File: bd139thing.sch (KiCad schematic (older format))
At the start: 24 parts, among them J1 Audio-Jack-3, J2 Jack-DC, Q1 PN2222, Q2 BD13916, Q3 BD13916, Q4 PN2222, Q5 BD13916, Q6 BD13916

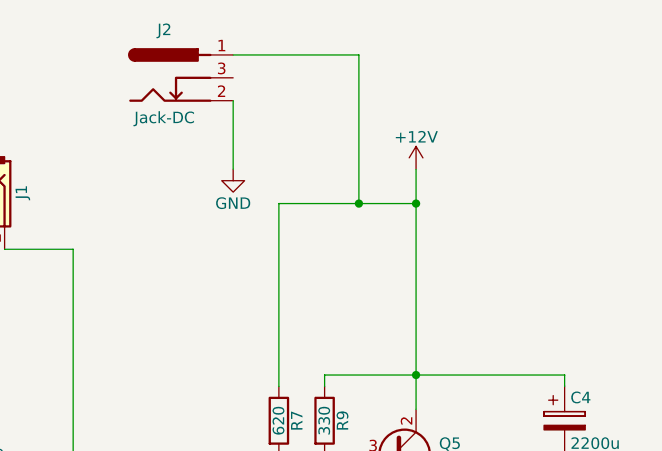
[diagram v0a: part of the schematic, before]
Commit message: r5p0 ok, improved placement on 75x75mm
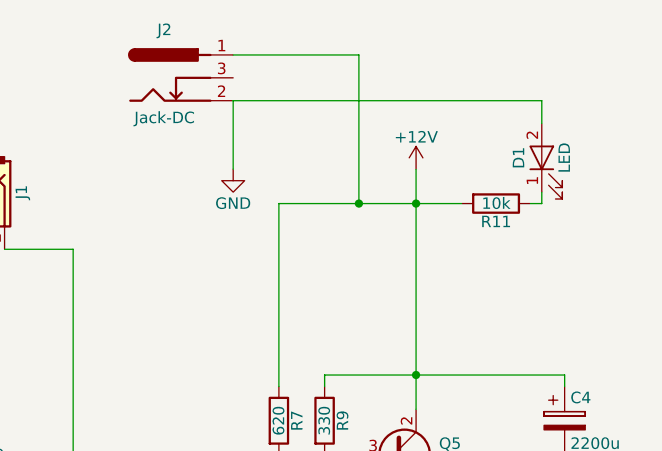
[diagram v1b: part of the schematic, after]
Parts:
- added D1: LED, LEDs:LED_D5.0mm, symbol LED
- added R11: 10k, Resistors_Universal:Resistor_SMD+THTuniversal_0805to1206_RM10_HandSoldering, symbol R
- R1, R2, R3, R4, R6, R7, R8, R9: footprint Resistors_Universal:Resistor_SMD+THTuniversal_0805to2512_RM10_HandSoldering -> Resistors_Universal:Resistor_SMD+THTuniversal_0805to1206_RM10_HandSoldering
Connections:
- net +12V: now also R11.2
- net GND: now also D1.2 (A)
- new net: D1.1 (K), R11.1
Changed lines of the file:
@@
 LIBS:contrib
 LIBS:valves
+LIBS:bd139thing-cache
 EELAYER 25 0
 EELAYER END
@@
 F 0 "R4" V 3080 3350 50  0000 C CNN
 F 1 "330" V 3000 3350 50  0000 C CNN
-F 2 "Resistors_Universal:Resistor_SMD+THTuniversal_0805to2512_RM10_HandSoldering" V 2930 3350 50  0001 C CNN
+F 2 "Resistors_Universal:Resistor_SMD+THTuniversal_0805to1206_RM10_HandSoldering" V 2930 3350 50  0001 C CNN
 F 3 "" H 3000 3350 50  0001 C CNN
 	1    3000 3350
@@
 F 0 "R2" V 2880 3350 50  0000 C CNN
 F 1 "620" V 2800 3350 50  0000 C CNN
-F 2 "Resistors_Universal:Resistor_SMD+THTuniversal_0805to2512_RM10_HandSoldering" V 2730 3350 50  0001 C CNN
+F 2 "Resistors_Universal:Resistor_SMD+THTuniversal_0805to1206_RM10_HandSoldering" V 2730 3350 50  0001 C CNN
 F 3 "" H 2800 3350 50  0001 C CNN
 	1    2800 3350
@@
 F 0 "R3" V 2880 4350 50  0000 C CNN
 F 1 "2.2k" V 2800 4350 50  0000 C CNN
-F 2 "Resistors_Universal:Resistor_SMD+THTuniversal_0805to2512_RM10_HandSoldering" V 2730 4350 50  0001 C CNN
+F 2 "Resistors_Universal:Resistor_SMD+THTuniversal_0805to1206_RM10_HandSoldering" V 2730 4350 50  0001 C CNN
 F 3 "" H 2800 4350 50  0001 C CNN
 	1    2800 4350
@@
 F 0 "R1" V 2580 3750 50  0000 C CNN
 F 1 "11" V 2500 3750 50  0000 C CNN
-F 2 "Resistors_Universal:Resistor_SMD+THTuniversal_0805to2512_RM10_HandSoldering" V 2430 3750 50  0001 C CNN
+F 2 "Resistors_Universal:Resistor_SMD+THTuniversal_0805to1206_RM10_HandSoldering" V 2430 3750 50  0001 C CNN
 F 3 "" H 2500 3750 50  0001 C CNN
 	1    2500 3750
@@
 F 0 "R9" V 5730 3300 50  0000 C CNN
 F 1 "330" V 5650 3300 50  0000 C CNN
-F 2 "Resistors_Universal:Resistor_SMD+THTuniversal_0805to2512_RM10_HandSoldering" V 5580 3300 50  0001 C CNN
+F 2 "Resistors_Universal:Resistor_SMD+THTuniversal_0805to1206_RM10_HandSoldering" V 5580 3300 50  0001 C CNN
 F 3 "" H 5650 3300 50  0001 C CNN
 	1    5650 3300
@@
 F 0 "R7" V 5530 3300 50  0000 C CNN
 F 1 "620" V 5450 3300 50  0000 C CNN
-F 2 "Resistors_Universal:Resistor_SMD+THTuniversal_0805to2512_RM10_HandSoldering" V 5380 3300 50  0001 C CNN
+F 2 "Resistors_Universal:Resistor_SMD+THTuniversal_0805to1206_RM10_HandSoldering" V 5380 3300 50  0001 C CNN
 F 3 "" H 5450 3300 50  0001 C CNN
 	1    5450 3300
@@
 F 0 "R8" V 5530 4300 50  0000 C CNN
 F 1 "2.2k" V 5450 4300 50  0000 C CNN
-F 2 "Resistors_Universal:Resistor_SMD+THTuniversal_0805to2512_RM10_HandSoldering" V 5380 4300 50  0001 C CNN
+F 2 "Resistors_Universal:Resistor_SMD+THTuniversal_0805to1206_RM10_HandSoldering" V 5380 4300 50  0001 C CNN
 F 3 "" H 5450 4300 50  0001 C CNN
 	1    5450 4300
@@
 F 0 "R6" V 5230 3700 50  0000 C CNN
 F 1 "11" V 5150 3700 50  0000 C CNN
-F 2 "Resistors_Universal:Resistor_SMD+THTuniversal_0805to2512_RM10_HandSoldering" V 5080 3700 50  0001 C CNN
+F 2 "Resistors_Universal:Resistor_SMD+THTuniversal_0805to1206_RM10_HandSoldering" V 5080 3700 50  0001 C CNN
 F 3 "" H 5150 3700 50  0001 C CNN
 	1    5150 3700
@@
 	1    0    0    -1
 $EndComp
+$Comp
+L R R11
+U 1 1 5D34F47E
+P 6400 2350
+F 0 "R11" V 6480 2350 50  0000 C CNN
+F 1 "10k" V 6400 2350 50  0000 C CNN
+F 2 "Resistors_Universal:Resistor_SMD+THTuniversal_0805to1206_RM10_HandSoldering" V 6330 2350 50  0001 C CNN
+F 3 "" H 6400 2350 50  0001 C CNN
+	1    6400 2350
+	0    1    1    0
+$EndComp
+$Comp
+L LED D1
+U 1 1 5D34F823
+P 6600 2150
+F 0 "D1" H 6600 2250 50  0000 C CNN
+F 1 "LED" H 6600 2050 50  0000 C CNN
+F 2 "LEDs:LED_D5.0mm" H 6600 2150 50  0001 C CNN
+F 3 "" H 6600 2150 50  0001 C CNN
+	1    6600 2150
+	0    -1   -1   0
+$EndComp
+Wire Wire Line
+	5250 1700 5800 1700
+Wire Wire Line
+	6600 1900 6600 2000
+Wire Wire Line
+	6600 2350 6600 2300
+Wire Wire Line
+	6550 2350 6600 2350
+Wire Wire Line
+	5250 1900 6600 1900
+Wire Wire Line
+	5250 2200 5250 1900
+Connection ~ 5800 2350
+Wire Wire Line
+	5800 1700 5800 2350
+Wire Wire Line
+	4050 2150 3900 2150
+Wire Wire Line
+	3400 4850 3400 4950
+Wire Wire Line
+	6050 4800 6050 4950
+Wire Wire Line
+	3900 2150 3900 2250
+Wire Wire Line
+	4550 2550 4550 3900
+Wire Wire Line
+	4250 2550 4550 2550
+Wire Wire Line
+	5450 4150 5450 4100
+Wire Wire Line
+	6700 4450 6700 4050
+Wire Wire Line
+	6700 3450 6700 3950
+Wire Wire Line
+	6700 3100 6700 3150
+Wire Wire Line
+	5650 3900 5750 3900
+Wire Wire Line
+	5650 3550 5650 3900
+Connection ~ 6050 4450
+Wire Wire Line
+	6050 4100 6050 4500
+Wire Wire Line
+	5450 4450 6700 4450
+Wire Wire Line
+	6050 3650 6050 3700
+Connection ~ 6050 3100
+Wire Wire Line
+	5650 3100 5650 3150
+Wire Wire Line
+	5650 3100 6700 3100
+Wire Wire Line
+	6050 2200 6050 3250
+Wire Wire Line
+	5750 3450 5650 3450
+Wire Wire Line
+	4550 3900 4650 3900
+Connection ~ 6050 2350
+Wire Wire Line
+	5450 2350 6250 2350
+Wire Wire Line
+	5450 3150 5450 2350
+Connection ~ 5450 3550
+Wire Wire Line
+	5450 3450 5450 3700
+Wire Wire Line
+	5150 3550 5650 3550
+Wire Wire Line
+	5150 3900 5150 3850
+Wire Wire Line
+	4950 3900 5150 3900
+Wire Wire Line
+	2800 4200 2800 4150
+Wire Wire Line
+	4050 4500 4050 4100
+Wire Wire Line
+	4050 3500 4050 4000
+Wire Wire Line
+	4050 3150 4050 3200
+Wire Wire Line
+	3000 3950 3100 3950
+Wire Wire Line
+	3000 3600 3000 3950
+Connection ~ 3400 4500
+Wire Wire Line
+	3400 4150 3400 4550
+Wire Wire Line
+	2800 4500 4050 4500
+Wire Wire Line
+	3400 3700 3400 3750
+Connection ~ 3400 3150
+Wire Wire Line
+	3000 3150 3000 3200
+Wire Wire Line
+	3000 3150 4050 3150
+Wire Wire Line
+	3400 2250 3400 3300
+Wire Wire Line
+	3100 3500 3000 3500
+Wire Wire Line
+	1900 3950 2000 3950
+Wire Wire Line
+	1900 2550 1900 3950
+Connection ~ 3400 2400
+Wire Wire Line
+	2800 2400 3400 2400
+Wire Wire Line
+	2800 3200 2800 2400
+Connection ~ 2800 3600
+Wire Wire Line
+	2800 3500 2800 3750
+Wire Wire Line
+	2500 3600 3000 3600
+Wire Wire Line
+	2500 3950 2500 3900
+Wire Wire Line
+	2300 3950 2500 3950
 Wire Wire Line
 	4150 2550 1900 2550
-Wire Wire Line
-	2300 3950 2500 3950
-Wire Wire Line
-	2500 3950 2500 3900
-Wire Wire Line
-	2500 3600 3000 3600
-Wire Wire Line
-	2800 3500 2800 3750
-Connection ~ 2800 3600
-Wire Wire Line
-	2800 3200 2800 2400
-Wire Wire Line
-	2800 2400 3400 2400
-Connection ~ 3400 2400
-Wire Wire Line
-	1900 2550 1900 3950
-Wire Wire Line
-	1900 3950 2000 3950
-Wire Wire Line
-	3100 3500 3000 3500
-Wire Wire Line
-	3400 2250 3400 3300
-Wire Wire Line
-	3000 3150 4050 3150
-Wire Wire Line
-	3000 3150 3000 3200
-Connection ~ 3400 3150
-Wire Wire Line
-	3400 3700 3400 3750
-Wire Wire Line
-	2800 4500 4050 4500
-Wire Wire Line
-	3400 4150 3400 4550
-Connection ~ 3400 4500
-Wire Wire Line
-	3000 3600 3000 3950
-Wire Wire Line
-	3000 3950 3100 3950
-Wire Wire Line
-	4050 3150 4050 3200
-Wire Wire Line
-	4050 3500 4050 4000
-Wire Wire Line
-	4050 4500 4050 4100
-Wire Wire Line
-	2800 4200 2800 4150
-Wire Wire Line
-	4950 3900 5150 3900
-Wire Wire Line
-	5150 3900 5150 3850
-Wire Wire Line
-	5150 3550 5650 3550
-Wire Wire Line
-	5450 3450 5450 3700
-Connection ~ 5450 3550
-Wire Wire Line
-	5450 3150 5450 2350
-Wire Wire Line
-	5450 2350 6050 2350
-Connection ~ 6050 2350
-Wire Wire Line
-	4550 3900 4650 3900
-Wire Wire Line
-	5750 3450 5650 3450
-Wire Wire Line
-	6050 2200 6050 3250
-Wire Wire Line
-	5650 3100 6700 3100
-Wire Wire Line
-	5650 3100 5650 3150
-Connection ~ 6050 3100
-Wire Wire Line
-	6050 3650 6050 3700
-Wire Wire Line
-	5450 4450 6700 4450
-Wire Wire Line
-	6050 4100 6050 4500
-Connection ~ 6050 4450
-Wire Wire Line
-	5650 3550 5650 3900
-Wire Wire Line
-	5650 3900 5750 3900
-Wire Wire Line
-	6700 3100 6700 3150
-Wire Wire Line
-	6700 3450 6700 3950
-Wire Wire Line
-	6700 4450 6700 4050
-Wire Wire Line
-	5450 4150 5450 4100
-Wire Wire Line
-	4250 2550 4550 2550
-Wire Wire Line
-	4550 2550 4550 3900
-Wire Wire Line
-	3900 2150 3900 2250
-Wire Wire Line
-	6050 4800 6050 4950
-Wire Wire Line
-	3400 4850 3400 4950
-Wire Wire Line
-	4050 2150 3900 2150
-Wire Wire Line
-	5250 1700 5800 1700
-Wire Wire Line
-	5800 1700 5800 2350
-Connection ~ 5800 2350
-Wire Wire Line
-	5250 2200 5250 1900
 $EndSCHEMATC

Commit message: prepare fixes p1
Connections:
- net GND: now also D1.1 (K), J1.1; no longer D1.2 (A), J1.3
- net at C1.1: now also J1.3; no longer J1.1
- net at R11.1: now also D1.2 (A); no longer D1.1 (K)
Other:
- moved on the sheet: D1
